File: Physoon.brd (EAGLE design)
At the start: 100 x 80 mm, 37 parts, among them IC2 74AHC1G125DBV, IC3 74AHC1G125DBV, M1 HX1, X1 BU-SMA-V

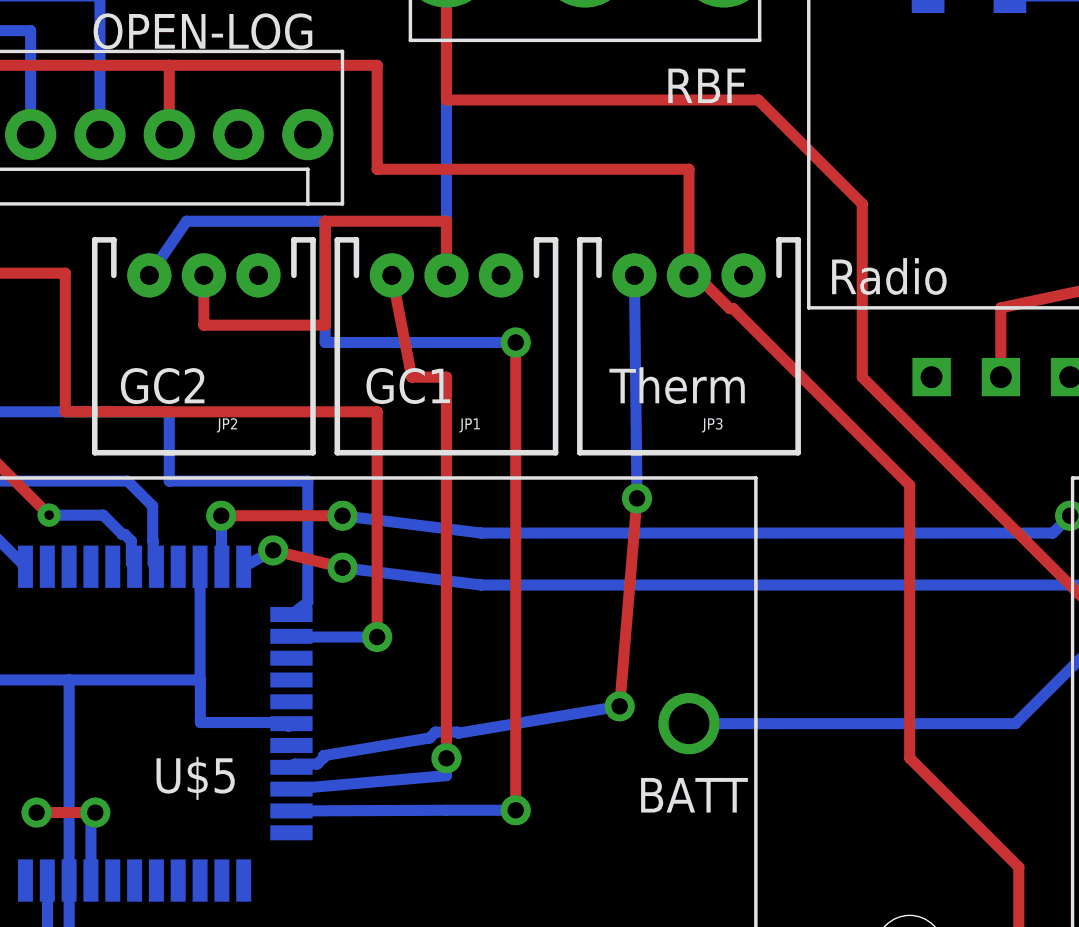
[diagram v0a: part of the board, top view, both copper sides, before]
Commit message: fix airwires and add fixed resistor for thermistor
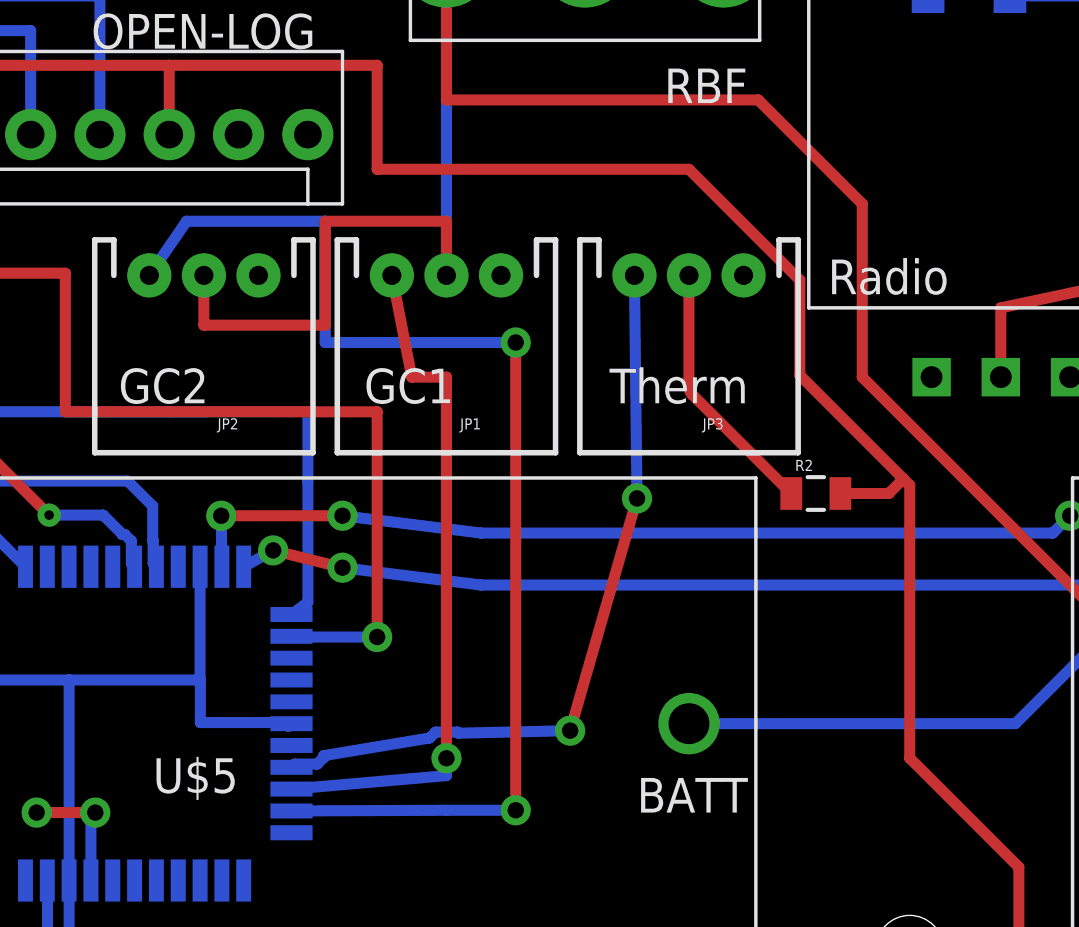
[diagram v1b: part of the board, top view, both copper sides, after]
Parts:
- added R2: (no value), SparkFun:0805
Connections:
- new net N$12: JP3.2, R2.1
- net VCC: now also R2.2; no longer JP3.2
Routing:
- net N$12: track 0.00 -> 9.52 mm
- net VCC: track 231.7 -> 234.0 mm
- net THERM: track 28.4 -> 27.6 mm
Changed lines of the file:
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@@
 <layer number="23" name="tOrigins" color="15" fill="1" visible="yes" active="yes"/>
 <layer number="24" name="bOrigins" color="15" fill="1" visible="yes" active="yes"/>
-<layer number="25" name="tNames" color="7" fill="1" visible="no" active="yes"/>
-<layer number="26" name="bNames" color="7" fill="1" visible="no" active="yes"/>
-<layer number="27" name="tValues" color="7" fill="1" visible="no" active="yes"/>
-<layer number="28" name="bValues" color="7" fill="1" visible="no" active="yes"/>
+<layer number="25" name="tNames" color="7" fill="1" visible="yes" active="yes"/>
+<layer number="26" name="bNames" color="7" fill="1" visible="yes" active="yes"/>
+<layer number="27" name="tValues" color="7" fill="1" visible="yes" active="yes"/>
+<layer number="28" name="bValues" color="7" fill="1" visible="yes" active="yes"/>
 <layer number="29" name="tStop" color="7" fill="3" visible="no" active="yes"/>
 <layer number="30" name="bStop" color="7" fill="6" visible="no" active="yes"/>
@@
 <layer number="42" name="bRestrict" color="1" fill="10" visible="no" active="yes"/>
 <layer number="43" name="vRestrict" color="2" fill="10" visible="no" active="yes"/>
-<layer number="44" name="Drills" color="7" fill="1" visible="no" active="yes"/>
+<layer number="44" name="Drills" color="7" fill="1" visible="yes" active="yes"/>
 <layer number="45" name="Holes" color="7" fill="1" visible="yes" active="yes"/>
 <layer number="46" name="Milling" color="3" fill="1" visible="no" active="yes"/>
@@
 <layer number="49" name="Reference" color="7" fill="1" visible="no" active="yes"/>
 <layer number="50" name="dxf" color="7" fill="1" visible="no" active="no"/>
-<layer number="51" name="tDocu" color="7" fill="1" visible="yes" active="yes"/>
-<layer number="52" name="bDocu" color="7" fill="1" visible="yes" active="yes"/>
+<layer number="51" name="tDocu" color="7" fill="1" visible="no" active="yes"/>
+<layer number="52" name="bDocu" color="7" fill="1" visible="no" active="yes"/>
 <layer number="53" name="tGND_GNDA" color="7" fill="9" visible="no" active="no"/>
 <layer number="54" name="bGND_GNDA" color="1" fill="9" visible="no" active="no"/>
@@
 <layer number="207" name="207bmp" color="8" fill="10" visible="no" active="yes"/>
 <layer number="208" name="208bmp" color="9" fill="10" visible="no" active="yes"/>
-<layer number="209" name="209bmp" color="1" fill="10" visible="yes" active="yes"/>
+<layer number="209" name="209bmp" color="1" fill="10" visible="no" active="yes"/>
 <layer number="210" name="210bmp" color="7" fill="1" visible="no" active="yes"/>
 <layer number="211" name="211bmp" color="7" fill="1" visible="no" active="yes"/>
@@
 <element name="R1" library="resistor" package="R0603" value="220" x="49" y="32"/>
 <element name="DIODE" library="Physoon" package="LILYPAD-WEARABLES_LED-1206" value="" x="52.17348125" y="75.005" rot="MR0"/>
+<element name="R2" library="SparkFun" package="0805" value="" x="46.558196875" y="56.695340625"/>
 </elements>
 <signals>
@@
 <via x="18" y="45" extent="1-16" drill="0.6"/>
 <contactref element="LED1" pad="C"/>
-<wire x1="27.34" y1="49.06" x2="23.19" y2="54.01" width="0" layer="19" extent="16-16"/>
 </signal>
 <signal name="PDI-DATA">
@@
 <contactref element="U$9" pad="1"/>
 <wire x1="7.62" y1="59.69" x2="22.86" y2="59.69" width="0.4064" layer="16"/>
-<wire x1="22.86" y1="59.69" x2="22.86" y2="57.15" width="0.4064" layer="16"/>
+<wire x1="22.86" y1="59.69" x2="27.94508125" y2="59.6925375" width="0.4064" layer="16"/>
 <wire x1="27.94" y1="57.15" x2="27.94" y2="52.705" width="0.4064" layer="16"/>
 <wire x1="27.94" y1="52.705" x2="27.34" y2="52.26" width="0.4064" layer="16"/>
-<wire x1="22.86" y1="57.15" x2="27.94" y2="57.15" width="0.4064" layer="16"/>
+<wire x1="27.94508125" y1="59.6925375" x2="27.94" y2="57.15" width="0.4064" layer="16"/>
 </signal>
 <signal name="PDI-CLK">
@@
 <contactref element="C3" pad="1"/>
 <contactref element="MPU" pad="3"/>
-<contactref element="JP3" pad="2"/>
 <contactref element="IC1" pad="9"/>
 <contactref element="IC1" pad="19"/>
@@
 <wire x1="22.86" y1="72.39" x2="30.48" y2="72.39" width="0.4064" layer="1"/>
 <wire x1="30.48" y1="72.39" x2="30.48" y2="68.58" width="0.4064" layer="1"/>
-<wire x1="30.48" y1="68.58" x2="41.91" y2="68.58" width="0.4064" layer="1"/>
-<wire x1="41.91" y1="68.58" x2="41.91" y2="64.69" width="0.4064" layer="1"/>
+<wire x1="41.91" y1="68.58" x2="30.48" y2="68.58" width="0.4064" layer="1"/>
 <wire x1="27.34" y1="48.26" x2="27.2304" y2="48.1504" width="0.4064" layer="16"/>
 <wire x1="63.5" y1="38.95" x2="66.72" y2="38.95" width="0.4064" layer="16"/>
@@
 <wire x1="21" y1="38" x2="54" y2="38" width="0.4064" layer="16"/>
 <wire x1="54" y1="38" x2="62.55" y2="38" width="0.4064" layer="16"/>
-<wire x1="43.4049875" y1="63.4708" x2="43.5292" y2="63.4708" width="0.4064" layer="1"/>
-<wire x1="43.5292" y1="63.4708" x2="50" y2="57" width="0.4064" layer="1"/>
-<wire x1="41.91" y1="64.69" x2="42.1857875" y2="64.69" width="0.4064" layer="1"/>
-<wire x1="42.1857875" y1="64.69" x2="43.4049875" y2="63.4708" width="0.4064" layer="1"/>
+<wire x1="49.768740625" y1="57.231259375" x2="45.971440625" y2="61.028559375" width="0.4064" layer="1"/>
+<wire x1="49.768740625" y1="57.231259375" x2="50" y2="57" width="0.4064" layer="1"/>
 <wire x1="50" y1="57" x2="50" y2="47" width="0.4064" layer="1"/>
 <wire x1="50" y1="47" x2="54" y2="43" width="0.4064" layer="1"/>
 <wire x1="54" y1="43" x2="54" y2="38" width="0.4064" layer="1"/>
 <via x="54" y="38" extent="1-16" drill="0.6"/>
+<contactref element="R2" pad="2"/>
+<wire x1="47.458196875" y1="56.695340625" x2="49.232821875" y2="56.695340625" width="0.4064" layer="1"/>
+<wire x1="49.232821875" y1="56.695340625" x2="49.768740625" y2="57.231259375" width="0.4064" layer="1"/>
+<wire x1="45.971440625" y1="61.028559375" x2="45.971440625" y2="64.518559375" width="0.4064" layer="1"/>
+<wire x1="45.971440625" y1="64.518559375" x2="41.91" y2="68.58" width="0.4064" layer="1"/>
 </signal>
 <signal name="N$1">
@@
 <wire x1="39.91" y1="64.69" x2="40.005" y2="56.515" width="0.4064" layer="16"/>
 <via x="40.005" y="56.515" extent="1-16" drill="0.6"/>
-<wire x1="40.005" y1="56.515" x2="39.37" y2="48.895" width="0.4064" layer="1"/>
-<via x="39.37" y="48.895" extent="1-16" drill="0.6"/>
-<wire x1="39.37" y1="48.895" x2="33.45846875" y2="47.90974375" width="0.4064" layer="16"/>
+<wire x1="40.005" y1="56.515" x2="37.5539" y2="48.003459375" width="0.4064" layer="1"/>
+<via x="37.5539" y="48.003459375" extent="1-16" drill="0.6"/>
+<wire x1="37.5539" y1="48.003459375" x2="33.45846875" y2="47.90974375" width="0.4064" layer="16"/>
 <wire x1="33.45846875" y1="47.90974375" x2="33.4178125" y2="47.9504" width="0.4064" layer="16"/>
 <wire x1="33.4178125" y1="47.9504" x2="32.6221875" y2="47.9504" width="0.4064" layer="16"/>
@@
 <wire x1="32.40614375" y1="47.73435625" x2="28.5214" y2="47.0869" width="0.4064" layer="16"/>
 <wire x1="28.5214" y1="47.0869" x2="28.5214" y2="47.0166625" width="0.4064" layer="16"/>
-<wire x1="28.5214" y1="47.0869" x2="28.5214" y2="47.0166625" width="0.4064" layer="16"/>
 <wire x1="28.5214" y1="47.0166625" x2="28.2833375" y2="46.7786" width="0.4064" layer="16"/>
 <wire x1="28.2833375" y1="46.7786" x2="27.4586" y2="46.7786" width="0.4064" layer="16"/>
@@
 <wire x1="21.150840625" y1="55.1914" x2="21.2333375" y2="55.1914" width="0.4064" layer="16"/>
 </signal>
+<signal name="N$12">
+<contactref element="JP3" pad="2"/>
+<contactref element="R2" pad="1"/>
+<wire x1="41.91" y1="64.69" x2="41.91" y2="60.611875" width="0.4064" layer="1"/>
+<wire x1="41.91" y1="60.611875" x2="42.02903125" y2="60.32450625" width="0.4064" layer="1" curve="45"/>
+<wire x1="42.02903125" y1="60.32450625" x2="45.658196875" y2="56.695340625" width="0.4064" layer="1"/>
+</signal>
 </signals>

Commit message: Add MCU power filtering, fix drill sizes to Sparkfun DRU
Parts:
- added C11, C15: 10uF, SparkFun:0805
- added C12, C16: 100nF, SparkFun:0805
- added L1: (no value), rcl:L2012C
- added L2: FB_0402, rc-master-smd:L0402
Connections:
- new net N$17: C15.2, C16.2, IC1.39, L2.1
- new net N$18: C11.1, C12.1, IC1.19, IC1.31, IC1.9, L1.1, L2.2
- net GND: now also C11.2, C12.2, C15.1, C16.1
- net VCC: now also L1.2; no longer IC1.19, IC1.31, IC1.39, IC1.9
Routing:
- net N$18: track 0.00 -> 32.2 mm
- net N$17: track 0.00 -> 32.0 mm
- net GND: track 21.4 -> 16.6 mm
- net VCC: track 234.0 -> 235.5 mm, vias 1 -> 2
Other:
- board text added: "Input"
